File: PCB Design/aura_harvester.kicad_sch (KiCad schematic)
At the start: 34 parts, among them J1 Conn_01x01_Pin, J2 Conn_01x01_Pin, J3 Conn_01x01_Pin, J4 Conn_01x01_Pin, J5 Conn_01x01_Pin, U1 ADG936BRUZ

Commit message: AURA PCB design
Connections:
- net GND: now also C10.2, C9.2, R2.2, U1.11 (GND), U1.13 (GND), U1.15 (GND), U1.16 (GND), U1.18 (GND), U1.20 (GND), U1.3 (GND), U1.5 (GND), U1.6 (GND)

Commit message: Completed Routing and Silkscreen
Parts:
- L2: footprint Capacitor_SMD:C_0402_1005Metric_Pad0.74x0.62mm_HandSolder -> Inductor_SMD:L_0402_1005Metric_Pad0.77x0.64mm_HandSolder
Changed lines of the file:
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@@
 			)
 		)
-		(property "Footprint" "Capacitor_SMD:C_0402_1005Metric_Pad0.74x0.62mm_HandSolder"
+		(property "Footprint" "Inductor_SMD:L_0402_1005Metric_Pad0.77x0.64mm_HandSolder"
 			(at 162.56 93.98 0)
 			(hide yes)

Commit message: modified SMA Antenna, RF diode Footprint, added testpoints
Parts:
- D1, D2, D3, D4, D5, D6, D8, D9: footprint Diode_SMD:D_SOD-523 -> Diode_SMD:D_SOD-323_HandSoldering
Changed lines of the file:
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@@
 			)
 		)
-		(property "Footprint" "Diode_SMD:D_SOD-523"
+		(property "Footprint" "Diode_SMD:D_SOD-323_HandSoldering"
 			(at 95.25 64.135 0)
 			(hide yes)
@@
 			)
 		)
-		(property "Footprint" "Diode_SMD:D_SOD-523"
+		(property "Footprint" "Diode_SMD:D_SOD-323_HandSoldering"
 			(at 184.15 64.135 0)
 			(hide yes)
@@
 			)
 		)
-		(property "Footprint" "Diode_SMD:D_SOD-523"
+		(property "Footprint" "Diode_SMD:D_SOD-323_HandSoldering"
 			(at 110.49 64.135 0)
 			(hide yes)
@@
 			)
 		)
-		(property "Footprint" "Diode_SMD:D_SOD-523"
+		(property "Footprint" "Diode_SMD:D_SOD-323_HandSoldering"
 			(at 153.67 64.135 0)
 			(hide yes)
@@
 			)
 		)
-		(property "Footprint" "Diode_SMD:D_SOD-523"
+		(property "Footprint" "Diode_SMD:D_SOD-323_HandSoldering"
 			(at 68.58 64.135 0)
 			(hide yes)
@@
 			)
 		)
-		(property "Footprint" "Diode_SMD:D_SOD-523"
+		(property "Footprint" "Diode_SMD:D_SOD-323_HandSoldering"
 			(at 139.7 64.135 0)
 			(hide yes)
@@
 			)
 		)
-		(property "Footprint" "Diode_SMD:D_SOD-523"
+		(property "Footprint" "Diode_SMD:D_SOD-323_HandSoldering"
 			(at 123.19 64.135 0)
 			(hide yes)
@@
 			)
 		)
-		(property "Footprint" "Diode_SMD:D_SOD-523"
+		(property "Footprint" "Diode_SMD:D_SOD-323_HandSoldering"
 			(at 173.99 64.135 0)
 			(hide yes)

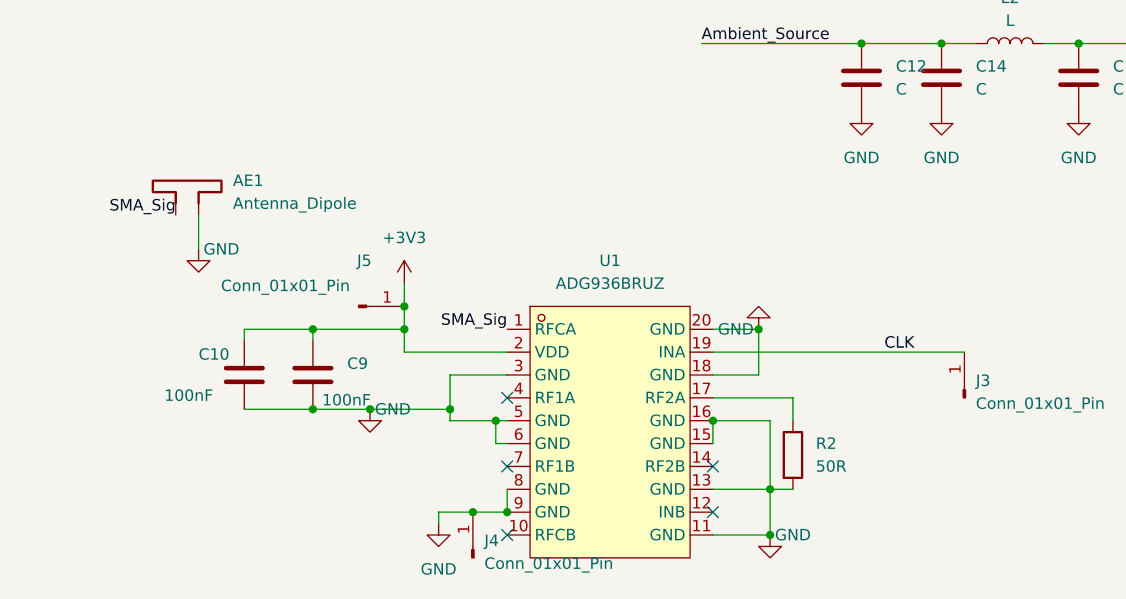
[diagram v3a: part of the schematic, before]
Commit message: modified SMA Antenna, RF diode Footprint, added testpoints
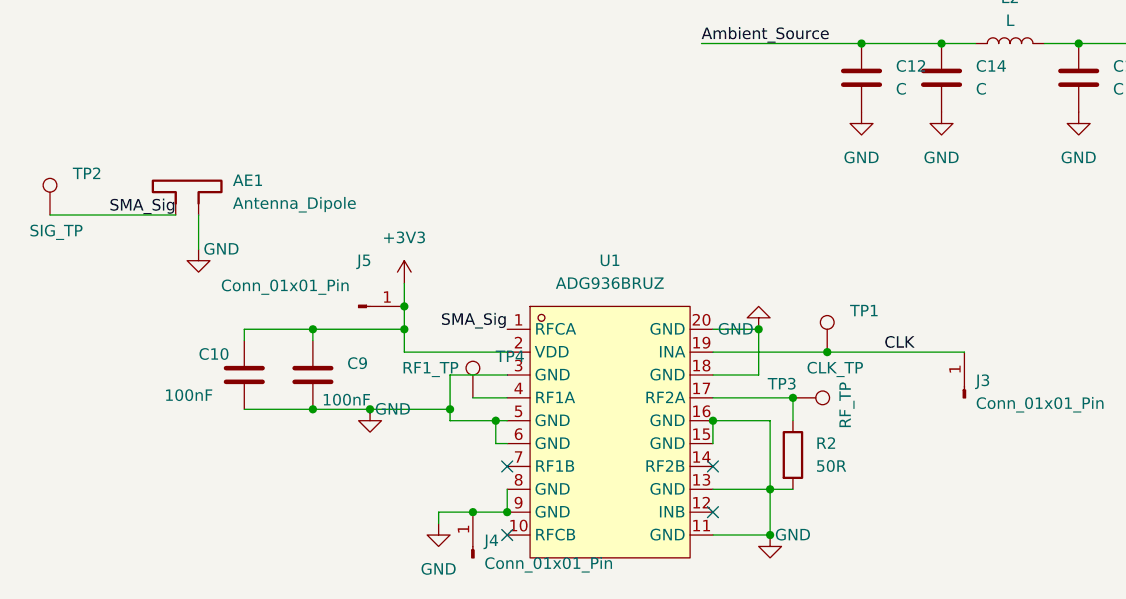
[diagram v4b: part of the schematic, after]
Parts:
- added TP1: CLK_TP, TestPoint:TestPoint_Pad_1.0x1.0mm, symbol Connector:TestPoint
- added TP2: SIG_TP, TestPoint:TestPoint_Pad_1.0x1.0mm, symbol Connector:TestPoint
- added TP3: RF_TP, TestPoint:TestPoint_Pad_1.0x1.0mm, symbol Connector:TestPoint
- added TP4: RF1_TP, TestPoint:TestPoint_Pad_1.0x1.0mm, symbol Connector:TestPoint
- AE1, AE2: footprint Connector_Coaxial:SMA_Amphenol_132134-10_Vertical -> Connector_Coaxial:SMA_Amphenol_132134_Vertical
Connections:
- net CLK: now also TP1.1
- net SMA_Sig: now also TP2.1
- net at R2.1, U1.17 (RF2A): now also TP3.1
- net at U1.4 (RF1A): now also TP4.1
- no-connect marks 5 -> 4
